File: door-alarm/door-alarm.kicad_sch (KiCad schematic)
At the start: 7 parts, among them U1 NE555P

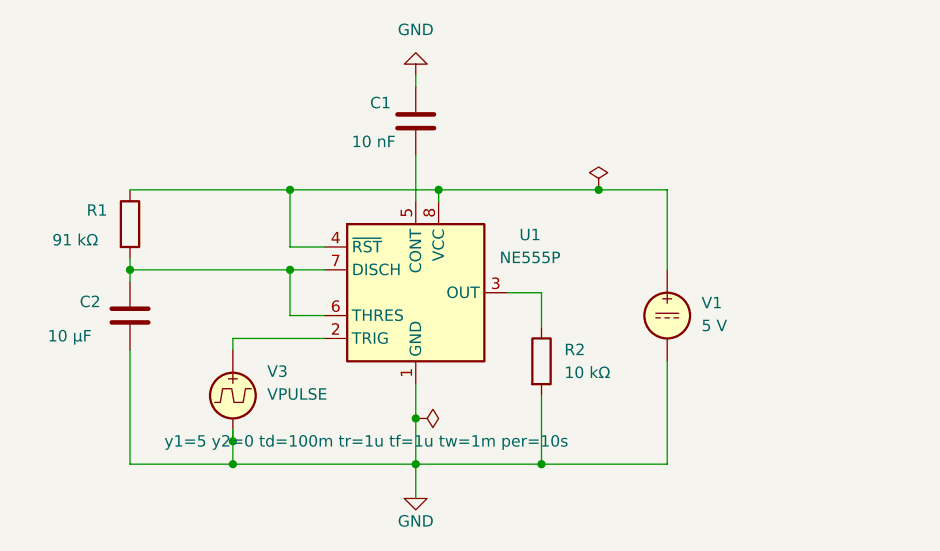
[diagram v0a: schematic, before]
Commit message: Finished the final schematic, layout and generated all necessary gerber and drill files.
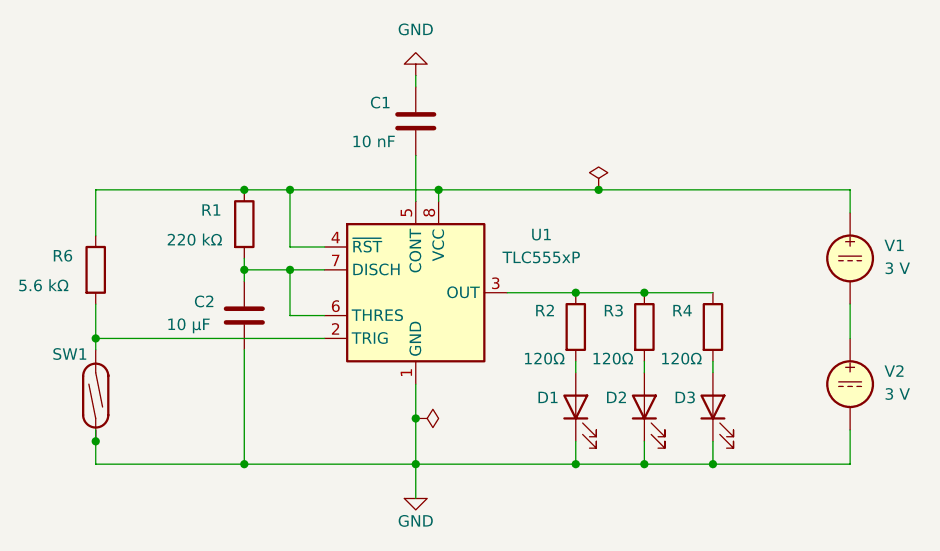
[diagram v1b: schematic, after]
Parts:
- removed U1: NE555P, Package_DIP:DIP-8_W7.62mm, symbol Timer:NE555P
- removed V3: VPULSE, symbol Simulation_SPICE:VPULSE
- added D1, D2, D3: LED, LED_THT:LED_D5.0mm, symbol Device:LED
- added R3, R4: 120Ω, Resistor_SMD:R_1206_3216Metric, symbol Device:R
- added R6: 5.6 kΩ, Resistor_SMD:R_1206_3216Metric, symbol Device:R
- added SW1: SW_Reed, Button_Switch_SMD:SW_SPDT_REED_MSDM-DT, symbol Switch:SW_Reed
- added U1: TLC555xP, Package_DIP:DIP-8_W7.62mm, symbol Timer:TLC555xP
- added V2: 3 V, Battery:BatteryHolder_Keystone_3002_1x2032, symbol Simulation_SPICE:VDC
- C1, C2: footprint (none) -> Capacitor_THT:C_Disc_D5.0mm_W2.5mm_P5.00mm
- R1: value 91 kΩ -> 220 kΩ; footprint (none) -> Resistor_SMD:R_1206_3216Metric
- R2: value 10 kΩ -> 120Ω; footprint (none) -> Resistor_SMD:R_1206_3216Metric
- V1: value 5 V -> 3 V; footprint (none) -> Battery:BatteryHolder_Keystone_3002_1x2032
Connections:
- net GND: now also D1.1 (K), D2.1 (K), D3.1 (K), SW1.1, U1.1 (GND), V2.2; no longer R2.2, V1.2
- net at R1.1, V1.1: now also R6.1, U1.4 (~{RST}), U1.8 (VCC)
- net at C2.1, R1.2: now also U1.6 (THRES), U1.7 (DISCH)
- net at R2.1: now also R3.1, R4.1, U1.3 (OUT)
- net at C1.2: now also U1.5 (CONT)
- new net: D2.2 (A), R3.2
- new net: D1.2 (A), R2.2
- new net: R6.2, SW1.2, U1.2 (TRIG)
- new net: V1.2, V2.1
- new net: D3.2 (A), R4.2
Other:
- moved on the sheet: C2, R1, V1

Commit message: Finished the second version of the alarm, which includes an active buzzer.
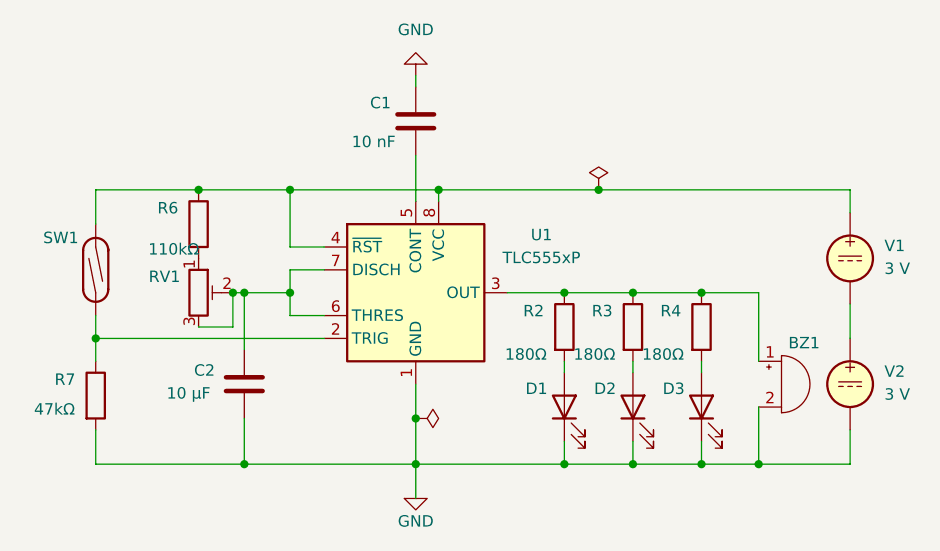
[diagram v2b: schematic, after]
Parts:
- removed R1: 220 kΩ, Resistor_SMD:R_1206_3216Metric, symbol Device:R
- added BZ1: Buzzer, Buzzer_Beeper:Buzzer_TDK_PS1240P02BT_D12.2mm_H6.5mm, symbol Device:Buzzer
- added R7: 47kΩ, Resistor_SMD:R_1206_3216Metric, symbol Device:R
- added RV1: R_Potentiometer_Trim, Potentiometer_THT:Potentiometer_Bourns_3266Z_Horizontal, symbol Device:R_Potentiometer_Trim
- R2, R3, R4: value 120Ω -> 180Ω
- R6: value 5.6 kΩ -> 110kΩ
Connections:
- net GND: now also BZ1.2 (-), R7.2; no longer SW1.1
- net at R6.1, U1.4 (~{RST}), U1.8 (VCC)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: now also SW1.2
- net at C2.1, U1.6 (THRES), U1.7 (DISCH): now also RV1.2, RV1.3
- net at R2.1, R3.1, R4.1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: now also BZ1.1 (+)
- new net: R6.2, RV1.1
- new net: R7.1, SW1.1, U1.2 (TRIG)
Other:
- moved on the sheet: C2, R2, R3, R4
